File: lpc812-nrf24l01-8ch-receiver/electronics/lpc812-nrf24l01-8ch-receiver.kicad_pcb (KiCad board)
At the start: 2 copper layers, 24 parts, among them J1 CH1, J2 CH2, J3 CH3/Rx, J4 CH4/Tx, J5 CH5, J6 CH6, J7 CH7, J8 CH8, SW1 BIND/ISP, U1 MCP1703A-3302_SOT23, U2 LPC812M101JDH20, U3 NRF24L01_Breakout, Y1 16MHz

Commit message: Work on initial layout
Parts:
- U3: footprint RF_Module:nRF24L01_Breakout -> nordic-semiconductor:nrf24l01-E01-ML01IPX
- moved J1 18.0 mm to (137.4, 68.5)
- moved J8 17.6 mm to (119.6, 68.5)
- moved SW1 15.0 mm to (122.2, 81.2), turned to 270 degrees
- moved C3 13.9 mm to (120.1, 88.1), turned to 0 degrees
- moved U3 13.0 mm to (118.6, 80.5), turned to 180 degrees
- moved J2 12.9 mm to (134.8, 68.5)
- moved J7 12.5 mm to (122.2, 68.5)
- moved RN1 10.3 mm to (131.0, 76.5)
- moved C4 10.0 mm to (132.9, 81.5)
- moved C2 8.20 mm to (133.8, 77.4), turned to 90 degrees
- moved C5 7.92 mm to (125.5, 86.8)
- moved J3 7.85 mm to (132.3, 68.5)
- moved Y1 7.76 mm to (136.0, 84.5)
- moved C7 7.66 mm to (135.9, 81.2)
- moved C6 7.63 mm to (135.9, 88.1)
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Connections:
- C6 pad 1: /XTALIN -> /XTALOUT
- C7 pad 1: /XTALOUT -> /XTALIN
- RN1 pad 1: /CH1 -> /CH4
- RN1 pad 2: /CH2 -> /CH3
- RN1 pad 3: /CH3-Rx -> /CH2
- RN1 pad 4: /CH4-Tx -> /CH1-Rx
- RN1 pad 5: Net-(J4-Pad3) -> Net-(J1-Pad3)
- RN1 pad 6: Net-(J3-Pad3) -> Net-(J2-Pad3)
- RN1 pad 7: Net-(J2-Pad3) -> Net-(J3-Pad3)
- RN1 pad 8: Net-(J1-Pad3) -> Net-(J4-Pad3)
- RN2 pad 1: /CH5 -> /CH8
- RN2 pad 2: /CH6 -> /CH7
- RN2 pad 3: /CH7 -> /CH6-Tx
- RN2 pad 4: /CH8 -> /CH5
- RN2 pad 5: Net-(J8-Pad3) -> Net-(J5-Pad3)
- RN2 pad 6: Net-(J7-Pad3) -> Net-(J6-Pad3)
- RN2 pad 7: Net-(J6-Pad3) -> Net-(J7-Pad3)
- RN2 pad 8: Net-(J5-Pad3) -> Net-(J8-Pad3)
- U2 pad 1: /CH8 -> /CH7
- U2 pad 10: /CH7 -> /CE
- U2 pad 11: /CH6 -> /LED
- U2 pad 12: /SCK -> /CH5
- U2 pad 17: /CH2 -> /CH4
- U2 pad 18: /CH1 -> /CH3
- U2 pad 19: /CH3-Rx -> /CH1-Rx
- U2 pad 2: /CE -> /CH8
- U2 pad 20: /CH5 -> /CH2
- U2 pad 4: /LED -> /IRQ
- U2 pad 5: /CH4-Tx -> /CH6-Tx
- U2 pad 6: /CSN -> /MISO
- U2 pad 8: /MISO -> /SCK
- U2 pad 9: /IRQ -> /CSN
- Y1 pad 1: /XTALOUT -> /XTALIN
- Y1 pad 2: /XTALIN -> /XTALOUT
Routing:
- net VDD: track 2.31 -> 25.9 mm
- net VCC: track 10.7 -> 31.7 mm, vias 0 -> 2
- net /CH5: track 0.00 -> 9.57 mm
- net /CH6: track 7.85 -> 0.00 mm
- net /MISO: track 0.00 -> 7.52 mm
- net /MOSI: track 0.00 -> 7.26 mm
- net /IRQ: track 0.00 -> 7.15 mm
- net /SCK: track 0.00 -> 7.00 mm
- net /CSN: track 0.00 -> 6.75 mm
- net /CH3-Rx: track 6.74 -> 0.00 mm
- net /CE: track 0.00 -> 6.64 mm
- net /BIND-ISP: track 0.00 -> 5.39 mm
- net /CH6-Tx: track 0.00 -> 5.06 mm
- net Net-(J4-Pad3): track 6.88 -> 2.10 mm
- net /CH4: track 0.00 -> 4.55 mm
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- added copper zone on B.Cu, net GND
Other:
- board outline added: 21 x 22 mm
- net class Default: trace_width 0.254 -> 0.2032

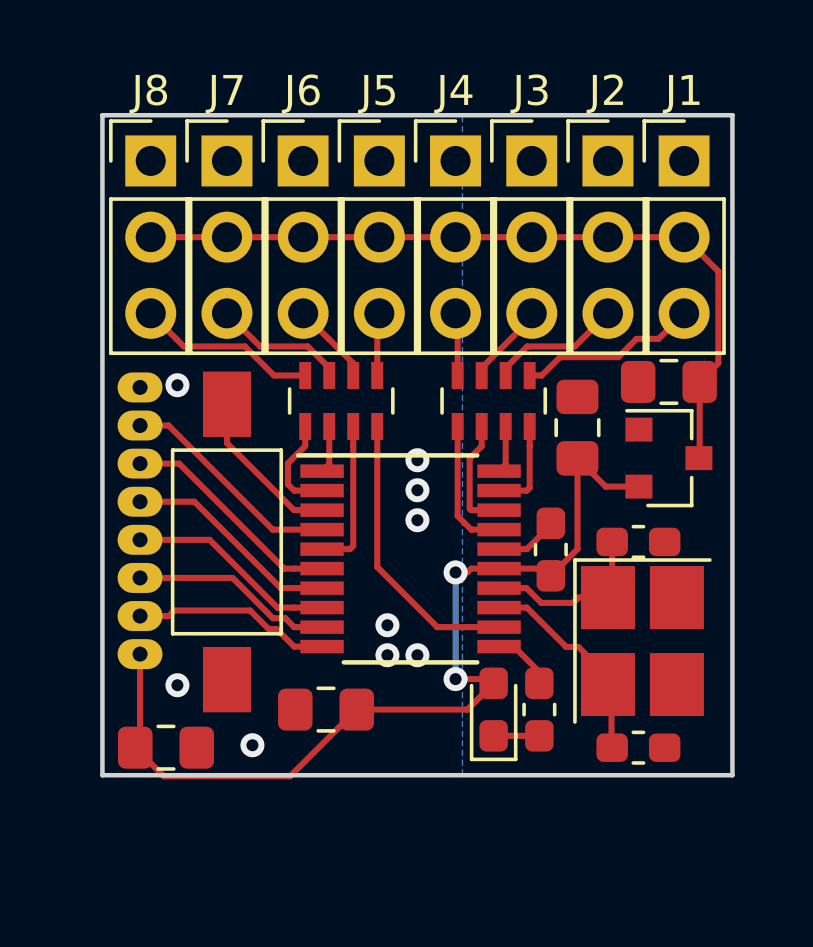
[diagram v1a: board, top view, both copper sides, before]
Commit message: Add correct symbol for nRF24 module
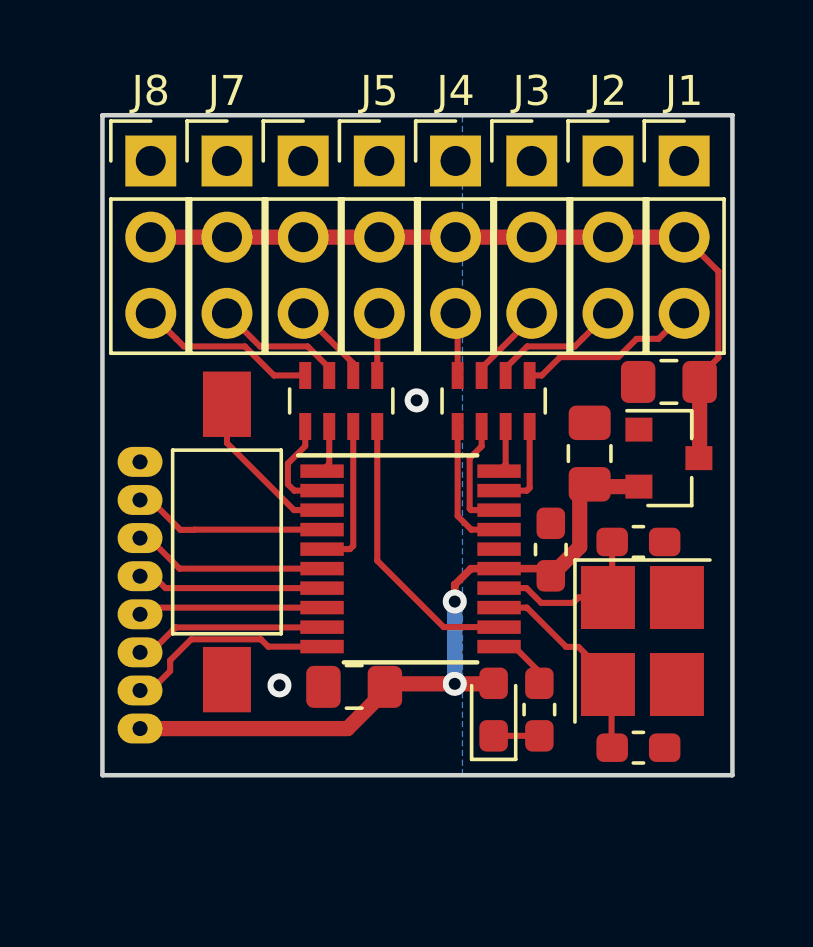
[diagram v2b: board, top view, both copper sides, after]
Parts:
- removed C2: 1u/16V, Capacitor_SMD:C_0805_2012Metric_Pad1.15x1.40mm_HandSolder
- C3, C5: value CP -> 47u/6.3V
- U3: value NRF24L01_Breakout -> NRF24L01_E01_ML01
- moved C5 12.3 mm to (134.2, 78.3), turned to 90 degrees
- moved C3 6.59 mm to (126.4, 86.1), turned to 180 degrees
- moved U3 2.48 mm to (118.6, 83.0), turned to 0 degrees
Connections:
- U3 pad 1: GND -> VCC
- U3 pad 2: VCC -> /CE
- U3 pad 3: /CE -> /CSN
- U3 pad 4: /CSN -> /SCK
- U3 pad 5: /SCK -> /MOSI
- U3 pad 6: /MOSI -> /MISO
- U3 pad 7: /MISO -> /IRQ
- U3 pad 8: /IRQ -> GND
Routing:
- net VCC: track 31.7 -> 24.5 mm
- net GND: track 2.12 -> 0.15 mm, vias 9 -> 2
- net /MISO: track 7.52 -> 6.49 mm
- net /MOSI: track 7.26 -> 6.23 mm
- net /SCK: track 7.00 -> 6.16 mm
- net /CSN: track 6.75 -> 6.06 mm
- net /IRQ: track 7.15 -> 6.48 mm
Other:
- rule trace_min: 0.2 -> 0.2032

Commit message: Tweak layout
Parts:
- Y1: value 16MHz -> 12 MHz
- moved C4 8.53 mm to (126.4, 87.0)
- moved C1 3.80 mm to (133.9, 78.2), turned to 270 degrees
- moved C5 2.69 mm to (136.8, 79.2), turned to 180 degrees
- moved D1 2.68 mm to (128.4, 87.0), turned to 270 degrees
- moved C3 2.23 mm to (124.4, 87.0), turned to 90 degrees
- moved C6 1.91 mm to (134.2, 87.1), turned to 180 degrees
- moved R1 1.74 mm to (131.0, 86.1), turned to 0 degrees
- moved U1 1.74 mm to (136.7, 76.7), turned to 90 degrees
- moved C7 1.56 mm to (134.3, 81.0), turned to 180 degrees
- moved Y1 0.58 mm to (135.5, 84.2), turned to 0 degrees
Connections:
- Y1 pad 1: /XTALIN -> /XTALOUT
- Y1 pad 2: /XTALOUT -> Net-(Y1-Pad2)
- Y1 pad 3: (no net) -> /XTALIN
- Y1 pad 4: (no net) -> Net-(Y1-Pad4)
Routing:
- net VDD: track 25.9 -> 12.7 mm
- net VCC: track 24.5 -> 37.6 mm, vias 2 -> 0
- net GND: track 0.15 -> 11.6 mm
- net /XTALIN: track 5.89 -> 8.35 mm
- net /XTALOUT: track 7.01 -> 5.87 mm
- net /CH5: track 9.45 -> 9.43 mm, vias 0 -> 2
- net Net-(J1-Pad3): track 6.01 -> 6.02 mm, vias 0 -> 1
- added copper zone on F.Cu, net VDD
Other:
- rule trace_min: 0.2032 -> 0.1524

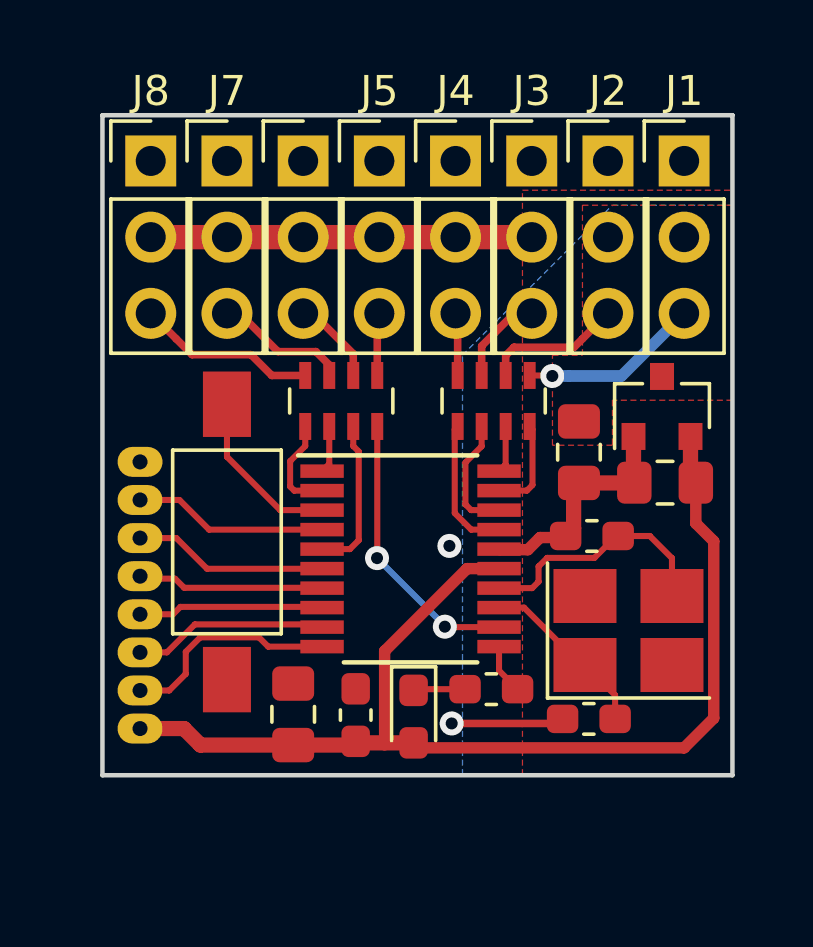
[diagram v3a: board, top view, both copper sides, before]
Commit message: Reposition the components
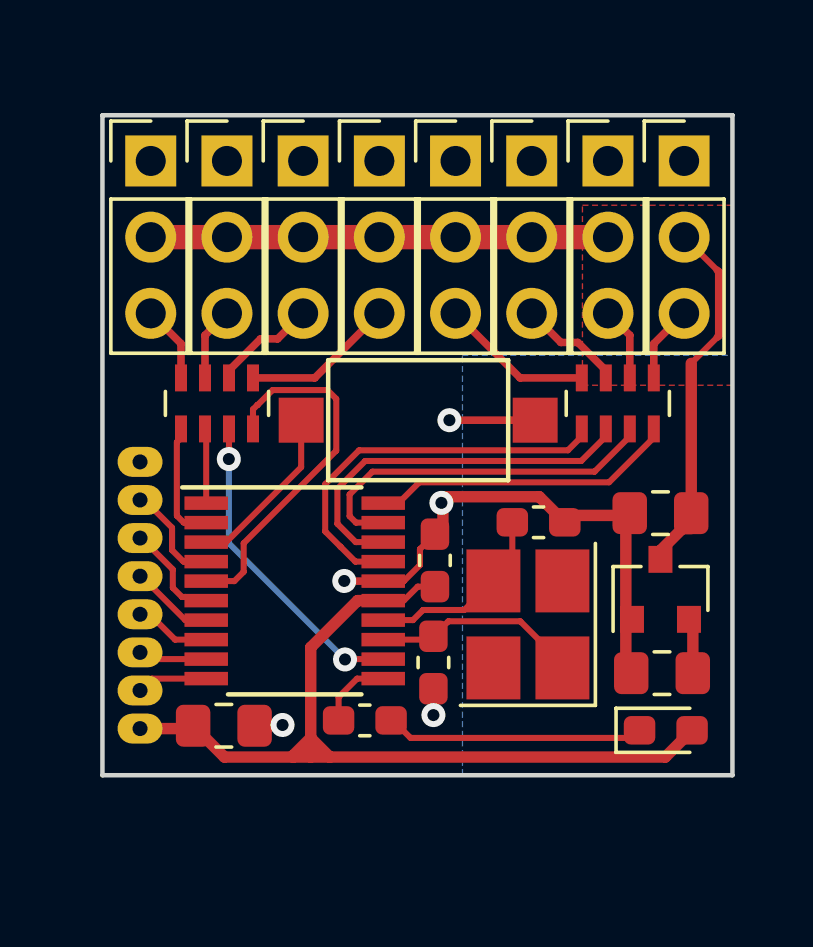
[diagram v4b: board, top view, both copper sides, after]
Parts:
- SW1: footprint Button_Switch_SMD:SW_SPST_FSMSM -> tact-switch:Tact switch 6x4x3
- moved D1 8.42 mm to (136.8, 87.5), turned to 0 degrees
- moved SW1 7.56 mm to (128.5, 77.2), turned to 0 degrees
- moved C5 6.35 mm to (136.7, 85.6)
- moved U1 6.10 mm to (136.6, 82.8)
- moved C4 5.79 mm to (129.1, 81.8)
- moved C6 5.51 mm to (129.0, 85.2), turned to 270 degrees
- moved R1 4.34 mm to (126.7, 87.2), turned to 180 degrees
- moved RN2 4.14 mm to (121.8, 76.6)
- moved RN1 4.14 mm to (135.2, 76.6)
- moved U2 4.01 mm to (124.4, 82.9)
- moved C1 3.39 mm to (136.6, 80.3), turned to 180 degrees
- moved Y1 3.36 mm to (132.2, 84.0), turned to 90 degrees
- moved C3 2.34 mm to (122.0, 87.4), turned to 0 degrees
- moved C7 1.84 mm to (132.5, 80.6), turned to 0 degrees
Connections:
- RN1 pad 3: /CH2 -> /CH2-Rx
- RN1 pad 4: /CH1-Rx -> /CH1
- RN2 pad 3: /CH6-Tx -> /CH6
- RN2 pad 4: /CH5 -> /CH5-Tx
- U2 pad 12: /CH5 -> /CH6
- U2 pad 19: /CH1-Rx -> /CH2-Rx
- U2 pad 20: /CH2 -> /CH1
- U2 pad 5: /CH6-Tx -> /CH5-Tx
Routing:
- net VDD: track 12.7 -> 27.4 mm
- net /CH2-Rx: track 0.00 -> 12.6 mm
- net /CH5-Tx: track 0.00 -> 12.2 mm
- net GND: track 11.6 -> 22.5 mm, vias 2 -> 5
- net /CH6: track 0.00 -> 10.8 mm, vias 0 -> 2
- net /CH1: track 0.00 -> 10.2 mm
- net /CH5: track 9.43 -> 0.00 mm, vias 2 -> 0
- net /CH3: track 4.02 -> 12.9 mm
- net /CH4: track 4.63 -> 13.4 mm
- net Net-(D1-Pad1): track 1.73 -> 8.77 mm
- net VCC: track 37.6 -> 31.5 mm
- net /CH6-Tx: track 5.21 -> 0.00 mm
- net /CE: track 7.00 -> 2.37 mm
- net /CSN: track 6.14 -> 2.30 mm
- net /SCK: track 6.18 -> 2.56 mm
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- removed copper zone on F.Cu, net GND

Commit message: Tweak layout
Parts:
- moved R1 6.32 mm to (133.1, 87.5)
- moved C6 0.64 mm to (129.1, 85.9)
- moved C7 0.56 mm to (132.0, 80.6), turned to 180 degrees
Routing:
- net VCC: track 31.5 -> 5.70 mm
- net VDD: track 27.4 -> 16.4 mm
- net Net-(D1-Pad1): track 8.77 -> 1.97 mm
- net /LED: track 2.52 -> 5.90 mm
- net /XTALIN: track 6.43 -> 7.07 mm
- net /XTALOUT: track 6.96 -> 7.49 mm
- net GND: track 22.5 -> 22.2 mm, vias 5 -> 4
- added copper zone on F.Cu, net VCC
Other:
- rule pad_to_mask_clearance: 0.2 -> 0.1016
- board text added: "."
- board text added: "BIND/ISP"
- board text added: "CH1"
- board text added: "CH3"
- board text added: "CH4"
- board text added: "CH6"
- board text added: "CH7"
- board text added: "CH8"
- board text added: "Rx2"
- board text added: "Tx5"

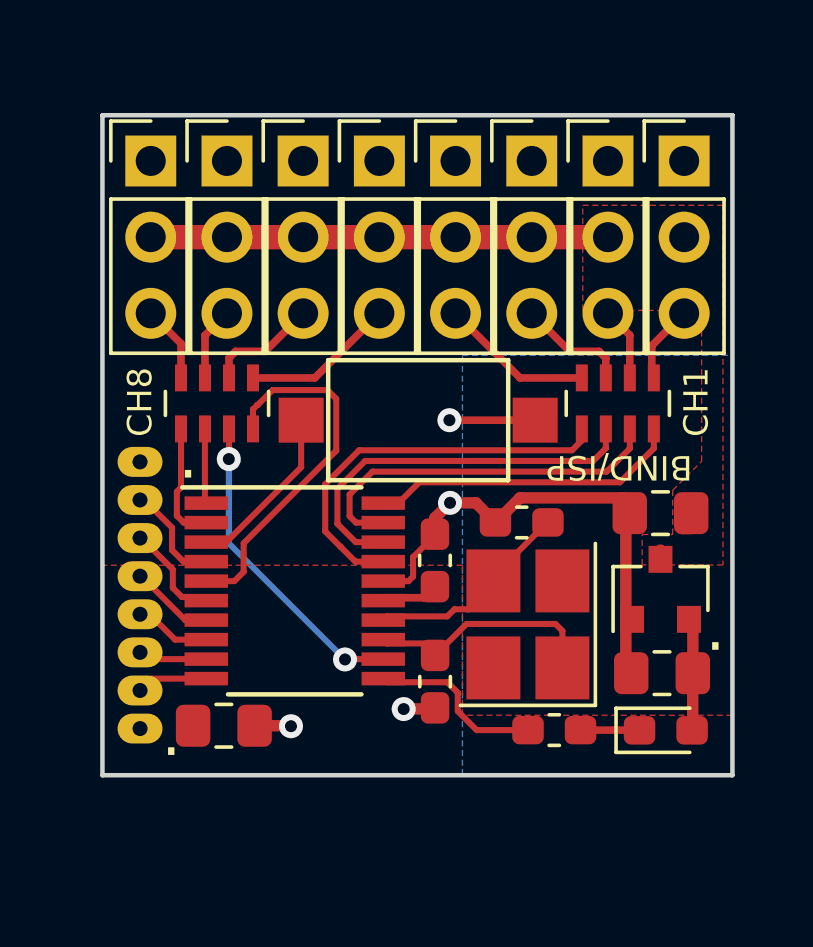
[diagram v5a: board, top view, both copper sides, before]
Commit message: Changel to 2520 crystal to shrink board to 21x21 mm
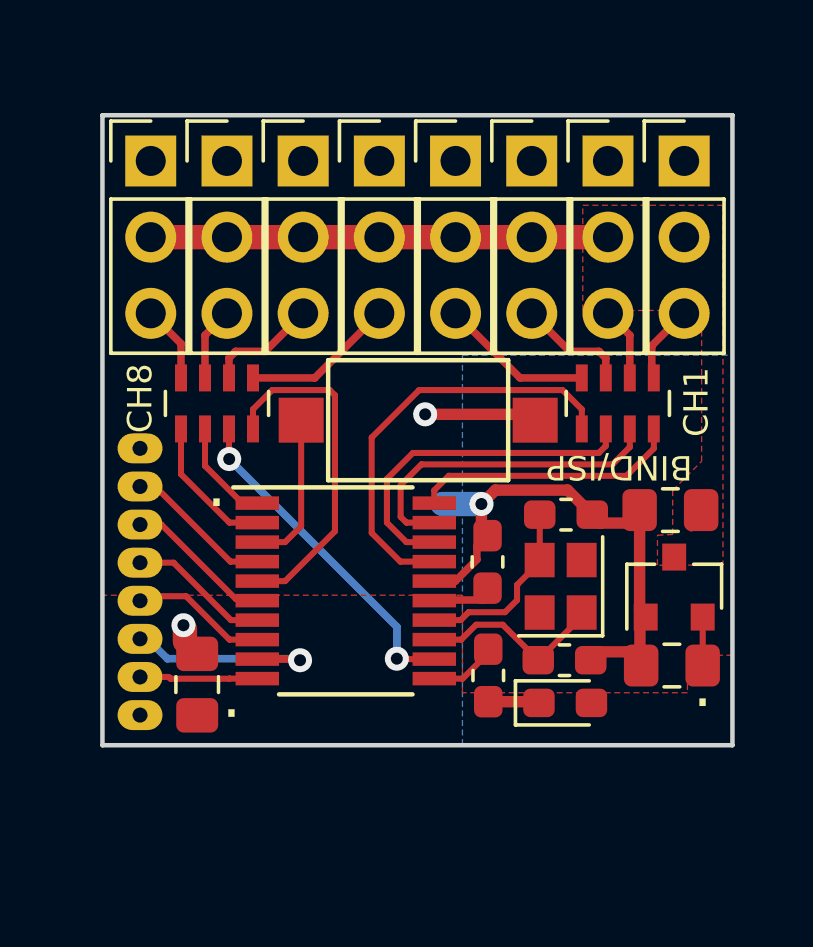
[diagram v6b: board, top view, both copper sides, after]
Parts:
- Y1: footprint Crystal:Crystal_SMD_3225-4Pin_3.2x2.5mm_HandSoldering -> Crystal:Crystal_SMD_2520-4Pin_2.5x2.0mm
- moved C6 4.37 mm to (133.4, 85.2), turned to 0 degrees
- moved D1 3.48 mm to (133.4, 86.6)
- moved R1 2.86 mm to (130.9, 85.7), turned to 90 degrees
- moved C4 1.75 mm to (130.8, 81.9)
- moved U2 1.70 mm to (126.1, 82.9)
- moved Y1 1.68 mm to (133.3, 82.7)
- moved C3 1.63 mm to (121.2, 86.0), turned to 90 degrees
- moved C7 1.50 mm to (133.5, 80.3), turned to 0 degrees
- moved U1 0.46 mm to (137.1, 82.7)
- moved U3 0.45 mm to (118.6, 82.5)
- moved C5 0.42 mm to (137.0, 85.3)
- moved C1 0.35 mm to (136.9, 80.2)
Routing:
- net /CSN: track 2.30 -> 7.07 mm, vias 0 -> 1
- net /LED: track 5.90 -> 2.19 mm
- net GND: track 22.2 -> 24.5 mm, vias 4 -> 3
- net /SCK: track 2.56 -> 4.57 mm
- net VCC: track 5.70 -> 3.73 mm
- net /MOSI: track 2.81 -> 4.70 mm
- net /CH2-Rx: track 12.8 -> 11.0 mm
- net /CE: track 2.37 -> 3.93 mm
- net /MISO: track 3.43 -> 4.96 mm
- net /CH3: track 13.1 -> 11.6 mm
- net /CH1: track 10.4 -> 8.98 mm
- net /IRQ: track 3.50 -> 4.95 mm
- net /XTALOUT: track 7.49 -> 6.35 mm
- net /CH7: track 2.49 -> 3.49 mm
- net /XTALIN: track 7.07 -> 6.20 mm
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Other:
- board size 21 x 22 mm -> 21 x 21 mm

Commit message: Optimize trace exit from pins
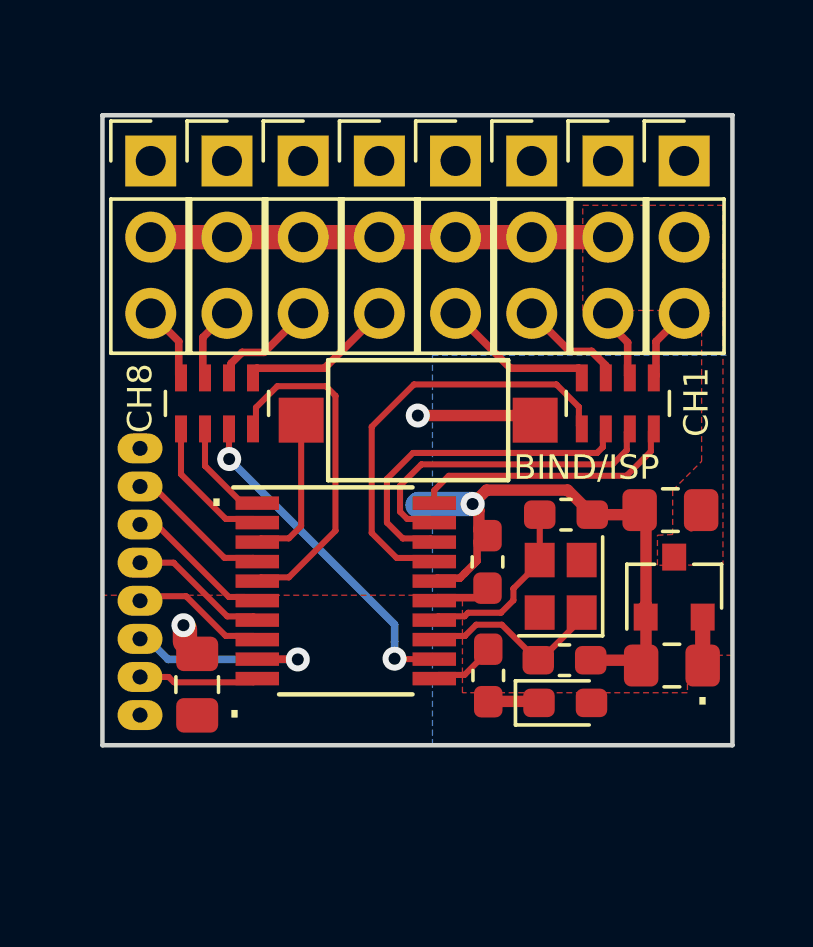
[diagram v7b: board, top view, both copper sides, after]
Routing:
- net GND: track 24.5 -> 25.1 mm
